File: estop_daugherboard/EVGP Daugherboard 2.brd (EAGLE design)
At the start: 82.6 x 94.1 mm, 41 parts, among them J1 JST-XH-02-PIN-LONG-PAD, J2 JST-XH-02-PIN-LONG-PAD, J3 JST-XH-03-PIN-LONG-PAD, J4 JST-XH-03-PIN-LONG-PAD, J5 AVR_SPI_PROG_3X2PTH, J6 UX60-MB-5S8, J7 4_XH_JST, Q1 N_FET2, Q2 N_FET1, U1 NL27WZ08USG, U2 ATMEGA32U4-AU, X1 TSX-3225 16.0000MF18X-AC0

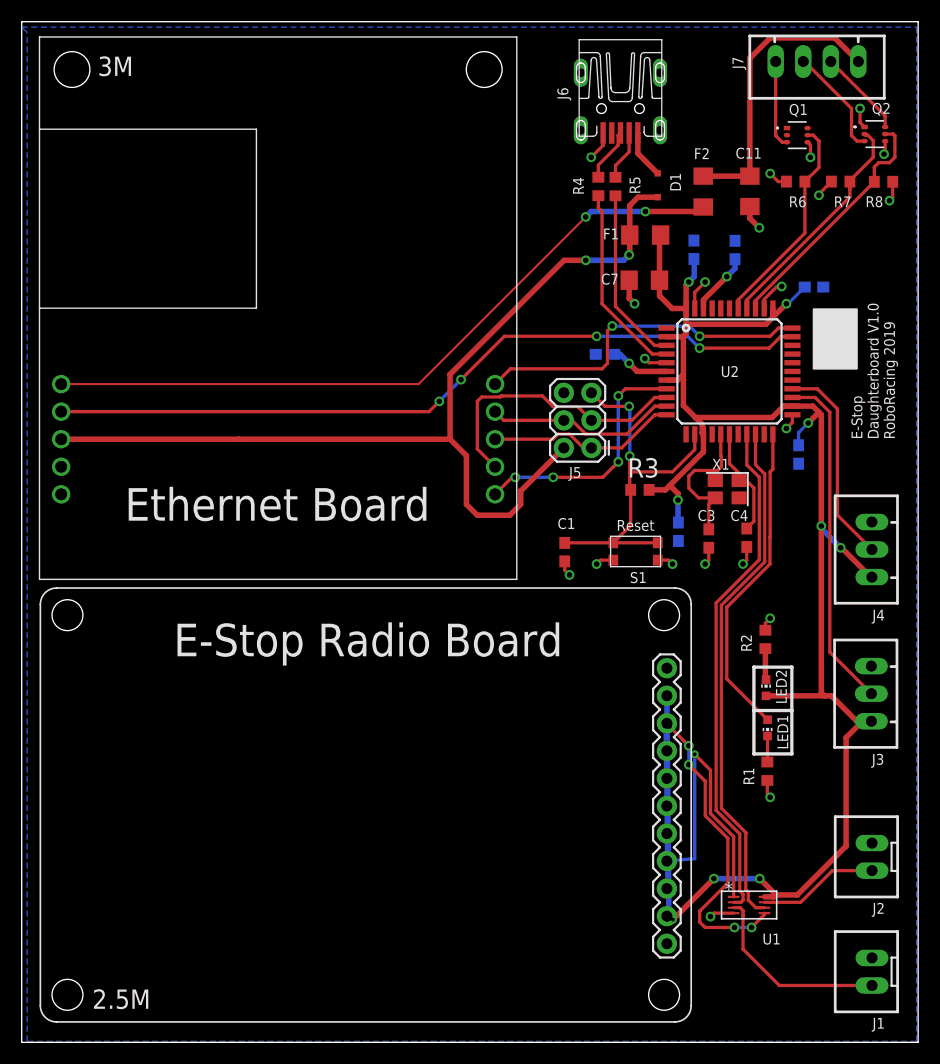
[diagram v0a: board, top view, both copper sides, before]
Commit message: IC silkscreens fixed and switched to merged library
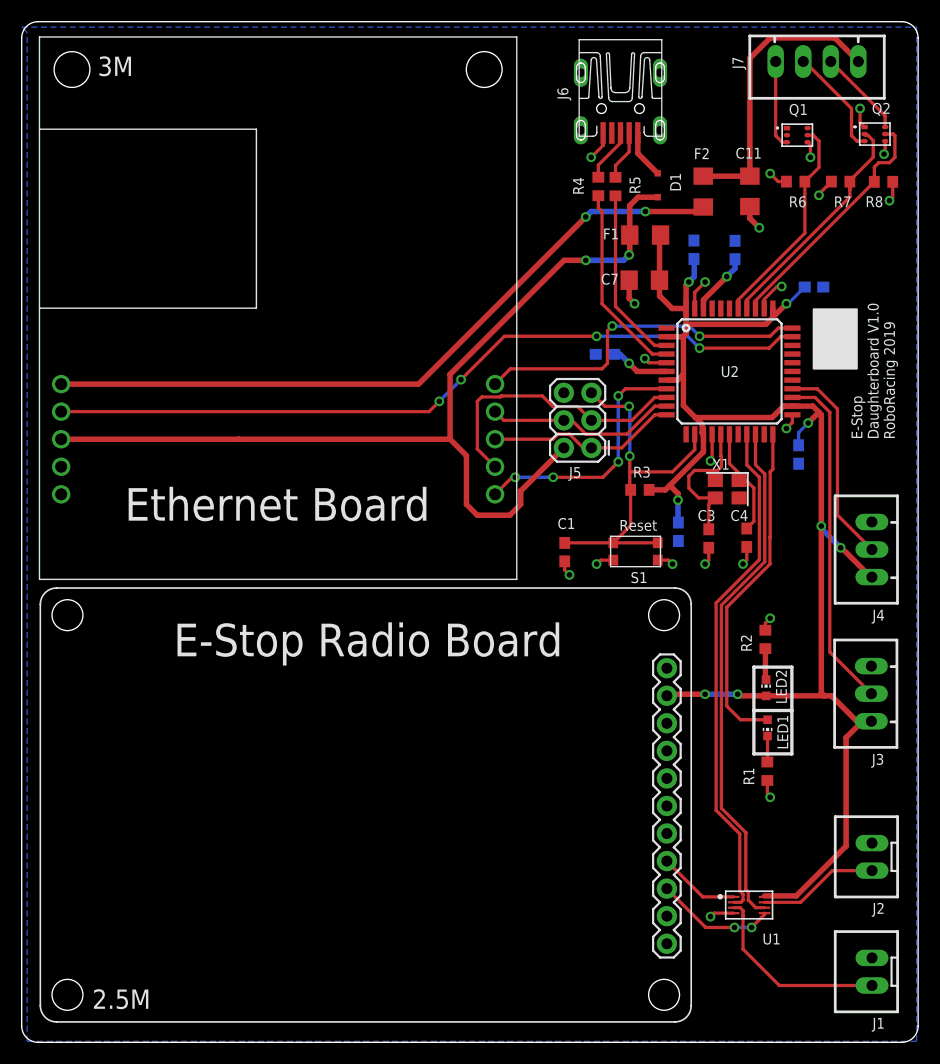
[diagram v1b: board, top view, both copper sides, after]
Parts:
- Q1, Q2: device DownloadedParts:SOT-363 -> Daughterboard-Stuff:SOT-363
- U1: device DownloadedFiles:US8_2P40X2P10 -> Daughterboard-Stuff:US8_2P40X2P10
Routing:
- net DRIVE_EN_RB: track 43.2 -> 11.1 mm, vias 5 -> 2
- net 5V: track 168.0 -> 144.7 mm, vias 9 -> 8
- net STEERING_EN_RB: track 26.8 -> 7.52 mm, vias 1 -> 0
- net GND: track 40.1 -> 42.6 mm, vias 21 -> 22
- net LED1: track 29.6 -> 31.1 mm
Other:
- outline, holes or cut-outs redrawn

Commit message: Fixed the routing widths
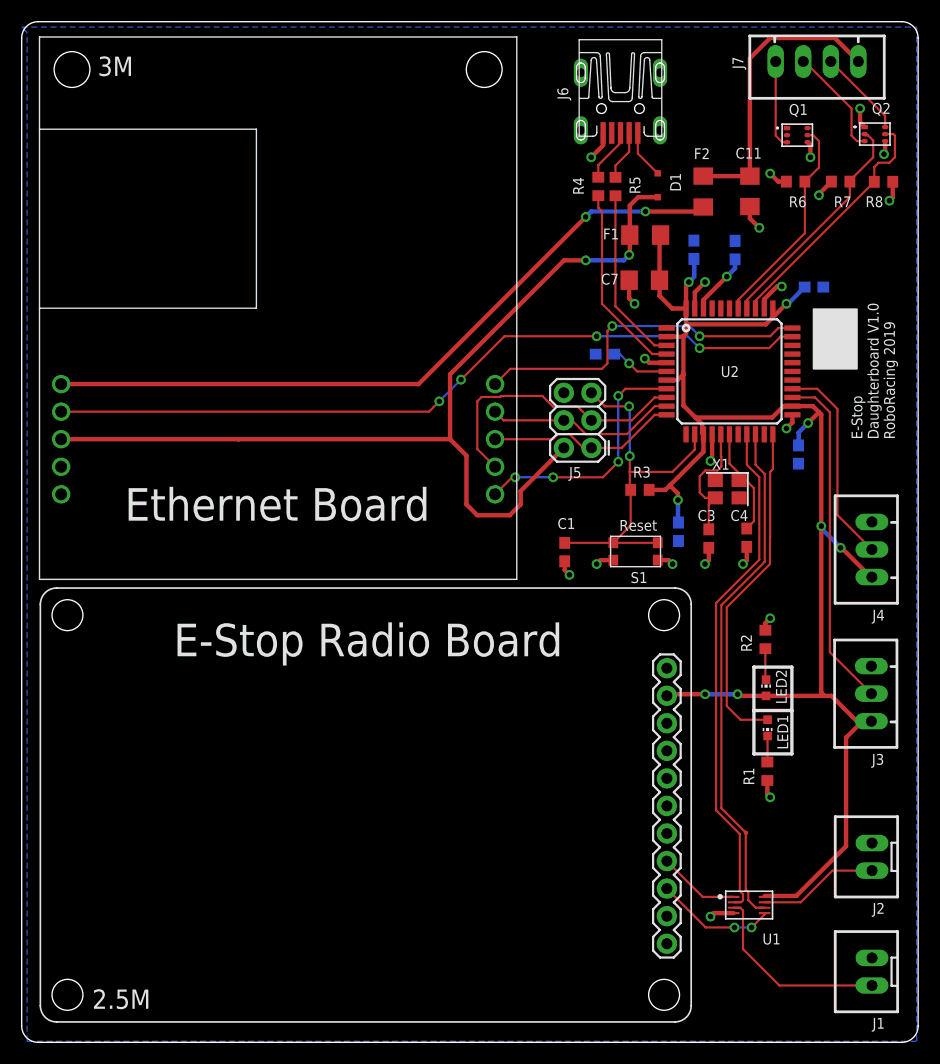
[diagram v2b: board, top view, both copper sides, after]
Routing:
- net XTAL2: track 13.4 -> 11.6 mm

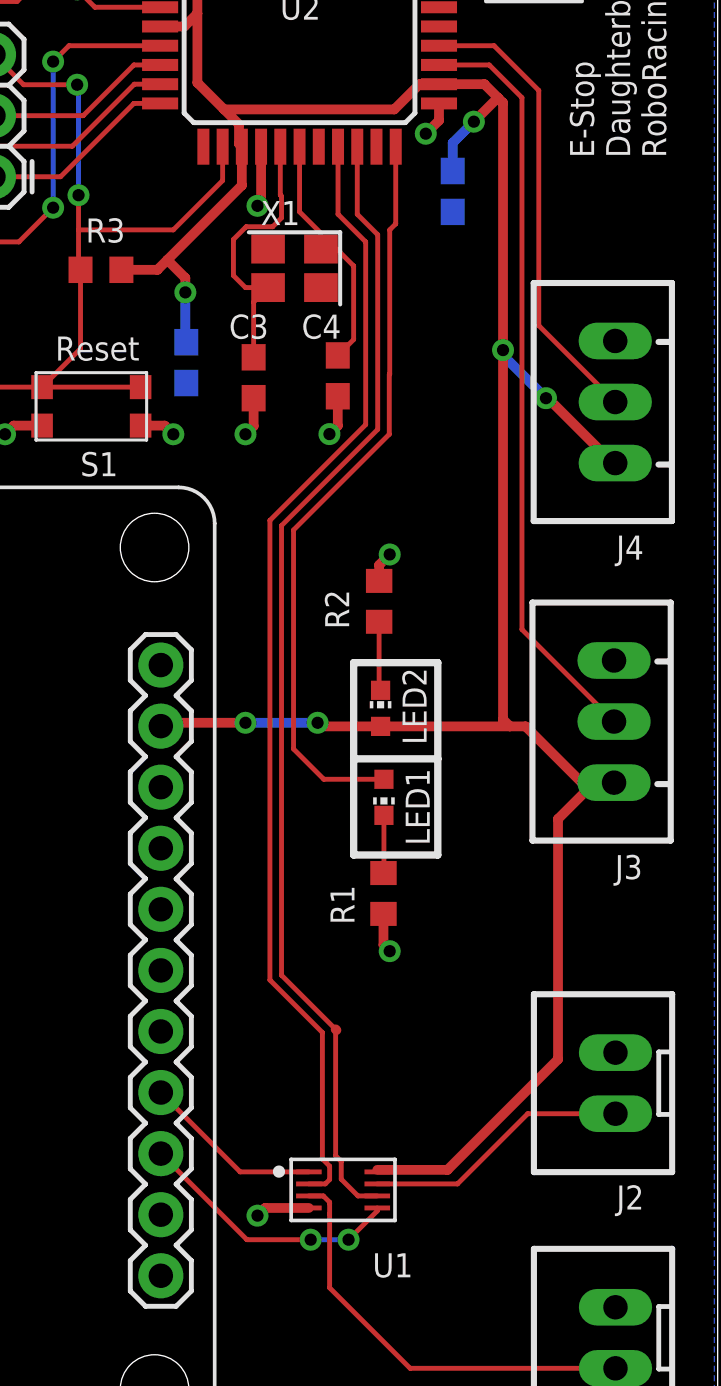
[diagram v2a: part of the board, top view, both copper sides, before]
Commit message: added enable_rb connections to atmega
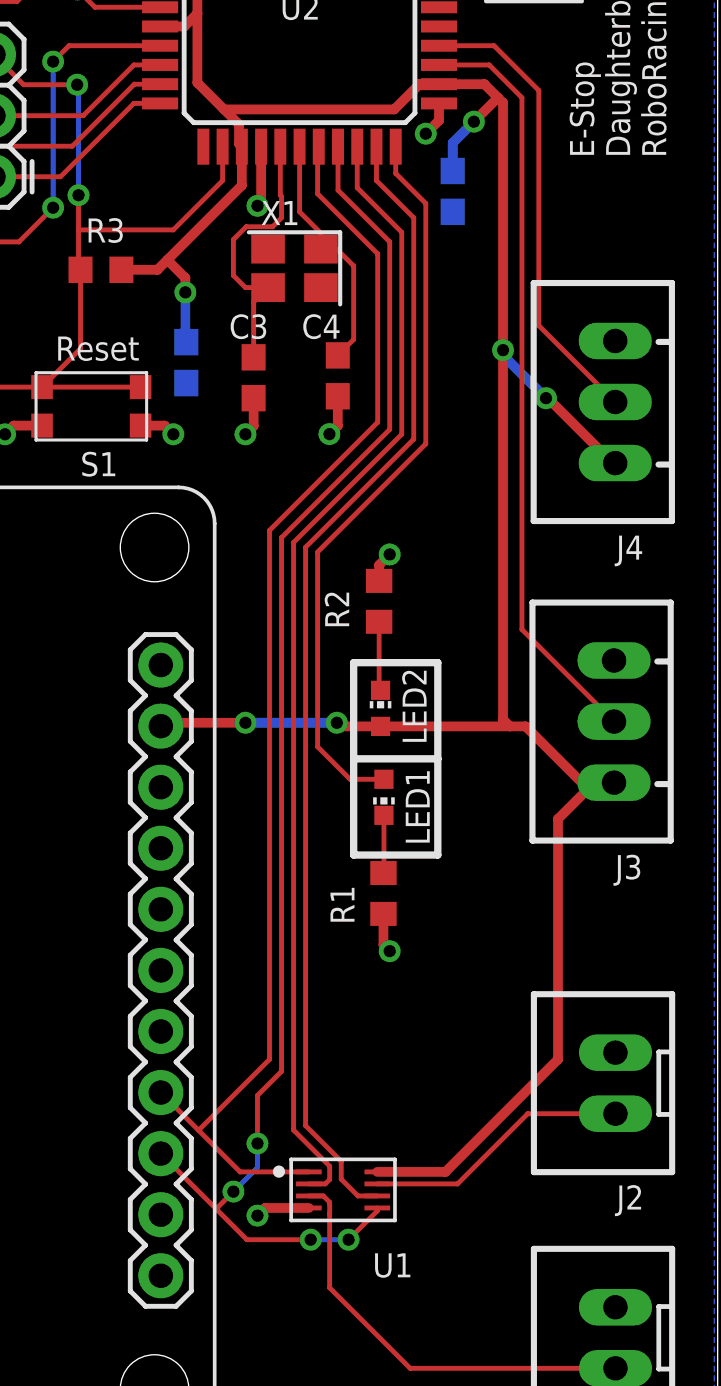
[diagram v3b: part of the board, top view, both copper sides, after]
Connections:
- net DRIVE_EN_DB: now also U2.21; no longer U2.20
- net DRIVE_EN_RB: now also U2.19
- net STEERING_EN_DB: now also U2.20; no longer U2.19
- net STEERING_EN_RB: now also U2.18
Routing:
- net DRIVE_EN_RB: track 11.1 -> 59.2 mm, vias 2 -> 4
- net STEERING_EN_RB: track 7.52 -> 52.6 mm
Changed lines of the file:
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@@
 <?xml version="1.0" encoding="utf-8"?>
 <!DOCTYPE eagle SYSTEM "eagle.dtd">
-<eagle version="9.5.1">
+<eagle version="9.5.0">
 <drawing>
 <settings>
@@
 <wire x1="76.5" y1="62.5" x2="76.5" y2="62.49934375" width="0.4064" layer="1"/>
 <wire x1="76.5" y1="62.49934375" x2="75.25" y2="61.24934375" width="0.4064" layer="1"/>
-<wire x1="77.4042" y1="7.9042" x2="74.4824" y2="7.9042" width="0.4064" layer="1"/>
-<wire x1="82" y1="12.5" x2="77.4042" y2="7.9042" width="0.4064" layer="1"/>
-<wire x1="74.62" y1="26.35" x2="72.15" y2="26.35" width="0.4064" layer="1"/>
-<wire x1="72.15" y1="26.35" x2="72" y2="26.5" width="0.4064" layer="1"/>
-<via x="72" y="26.5" extent="1-16" drill="0.508"/>
-<wire x1="72" y1="26.5" x2="69" y2="26.5" width="0.4064" layer="16"/>
+<wire x1="74.62" y1="26.35" x2="72.95" y2="26.35" width="0.4064" layer="1"/>
+<wire x1="72.95" y1="26.35" x2="72.8" y2="26.5" width="0.4064" layer="1"/>
+<via x="72.8" y="26.5" extent="1-16" drill="0.508"/>
+<wire x1="72.8" y1="26.5" x2="69" y2="26.5" width="0.4064" layer="16"/>
 <via x="69" y="26.5" extent="1-16" drill="0.508"/>
 <wire x1="69" y1="26.5" x2="65.62" y2="26.5" width="0.4064" layer="1"/>
 <wire x1="65.62" y1="26.5" x2="65.48" y2="26.36" width="0.4064" layer="1"/>
-<wire x1="74.4824" y1="7.9042" x2="74.4824" y2="7.82" width="0" layer="19" extent="1-1"/>
+<wire x1="77.32" y1="7.82" x2="74.4824" y2="7.82" width="0.4064" layer="1"/>
+<wire x1="82" y1="12.5" x2="77.32" y2="7.82" width="0.4064" layer="1"/>
 </signal>
 <signal name="MCU_RST">
@@
 <contactref element="LED1" pad="A"/>
 <contactref element="U2" pad="22"/>
-<wire x1="74.76" y1="24.15" x2="72.26" y2="24.15" width="0.2032" layer="1"/>
-<wire x1="72.26" y1="24.15" x2="71" y2="25.41" width="0.2032" layer="1"/>
-<wire x1="71" y1="34.5175" x2="74.9826" y2="38.5001" width="0.2032" layer="1"/>
-<wire x1="74.9826" y1="40.9826" x2="75" y2="41" width="0.2032" layer="1"/>
-<wire x1="74.9826" y1="38.5001" x2="74.9826" y2="40.9826" width="0.2032" layer="1"/>
-<wire x1="75" y1="47" x2="75" y2="41" width="0.2032" layer="1"/>
-<wire x1="71" y1="25.41" x2="71" y2="34.5175" width="0.2032" layer="1"/>
-<wire x1="75.25" y1="50.46" x2="75.25" y2="47.25" width="0.2032" layer="1"/>
-<wire x1="75.25" y1="47.25" x2="75" y2="47" width="0.2032" layer="1"/>
+<wire x1="74.76" y1="24.15" x2="73.35" y2="24.15" width="0.2032" layer="1"/>
+<wire x1="73.35" y1="24.15" x2="72" y2="25.5" width="0.2032" layer="1"/>
+<wire x1="75.25" y1="49.35" x2="75.25" y2="50.46" width="0.2032" layer="1"/>
+<wire x1="72" y1="25.5" x2="72" y2="33.6" width="0.2032" layer="1"/>
+<wire x1="72" y1="33.6" x2="76.5" y2="38.1" width="0.2032" layer="1"/>
+<wire x1="76.5" y1="38.1" x2="76.5" y2="48.1" width="0.2032" layer="1"/>
+<wire x1="76.5" y1="48.1" x2="75.25" y2="49.35" width="0.2032" layer="1"/>
 </signal>
 <signal name="STACK_MCU1">
@@
 <wire x1="74.4824" y1="6.195" x2="74.4824" y2="6.32" width="0.2032" layer="1"/>
 <wire x1="71.7126" y1="5" x2="69.06" y2="5" width="0.2032" layer="1"/>
-<wire x1="69.06" y1="5" x2="65.48" y2="8.58" width="0.2032" layer="1"/>
+<wire x1="69.06" y1="5" x2="67.78" y2="6.28" width="0.2032" layer="1"/>
+<contactref element="U2" pad="19"/>
+<wire x1="67.78" y1="6.28" x2="65.48" y2="8.58" width="0.2032" layer="1"/>
+<wire x1="67.78" y1="6.28" x2="68.5" y2="7" width="0.2032" layer="1"/>
+<via x="68.5" y="7" extent="1-16" drill="0.508"/>
+<wire x1="69.5" y1="8" x2="69.5" y2="9" width="0.2032" layer="16"/>
+<wire x1="69.5" y1="8" x2="68.5" y2="7" width="0.2032" layer="16"/>
+<via x="69.5" y="9" extent="1-16" drill="0.508"/>
+<wire x1="69.5" y1="9" x2="69.5" y2="11" width="0.2032" layer="1"/>
+<wire x1="69.5" y1="11" x2="70.5" y2="12" width="0.2032" layer="1"/>
+<wire x1="70.5" y1="12" x2="70.5" y2="34.2" width="0.2032" layer="1"/>
+<wire x1="70.5" y1="34.2" x2="75" y2="38.7" width="0.2032" layer="1"/>
+<wire x1="72.85" y1="48.65" x2="72.85" y2="50.46" width="0.2032" layer="1"/>
+<wire x1="75" y1="38.7" x2="75" y2="46.5" width="0.2032" layer="1"/>
+<wire x1="75" y1="46.5" x2="72.85" y2="48.65" width="0.2032" layer="1"/>
 </signal>
 <signal name="STEERING_EN_RB">
@@
 <contactref element="RADIO" pad="4"/>
 <wire x1="71.6376" y1="7.82" x2="68.78" y2="7.82" width="0.2032" layer="1"/>
-<wire x1="68.78" y1="7.82" x2="65.48" y2="11.12" width="0.2032" layer="1"/>
+<wire x1="68.78" y1="7.82" x2="67.05" y2="9.55" width="0.2032" layer="1"/>
+<contactref element="U2" pad="18"/>
+<wire x1="67.05" y1="9.55" x2="65.48" y2="11.12" width="0.2032" layer="1"/>
+<wire x1="67.05" y1="9.55" x2="70" y2="12.5" width="0.2032" layer="1"/>
+<wire x1="70" y1="34.5" x2="74.5" y2="39" width="0.2032" layer="1"/>
+<wire x1="74.5" y1="39" x2="74.5" y2="46" width="0.2032" layer="1"/>
+<wire x1="74.5" y1="46" x2="72" y2="48.5" width="0.2032" layer="1"/>
+<wire x1="72" y1="48.5" x2="72" y2="50.41" width="0.2032" layer="1"/>
+<wire x1="72" y1="50.41" x2="72.05" y2="50.46" width="0.2032" layer="1"/>
+<wire x1="70" y1="12.5" x2="70" y2="34.5" width="0.2032" layer="1"/>
 </signal>
 <signal name="DRIVE_EN_DB">
 <contactref element="U1" pad="6"/>
-<contactref element="U2" pad="20"/>
-<wire x1="73.65" y1="50.46" x2="73.65" y2="47.65" width="0.2032" layer="1"/>
-<wire x1="73.65" y1="47.65" x2="74.5" y2="46.8" width="0.2032" layer="1"/>
-<wire x1="74.5" y1="46.8" x2="74.5" y2="38.7" width="0.2032" layer="1"/>
-<wire x1="74.5" y1="38.7" x2="70.5" y2="34.7" width="0.2032" layer="1"/>
-<wire x1="70.5" y1="16" x2="70.5" y2="34.7" width="0.2032" layer="1"/>
 <wire x1="74.4824" y1="6.82" x2="73.68" y2="6.82" width="0.2032" layer="1"/>
-<wire x1="72.7838" y1="13.7162" x2="72.75" y2="13.75" width="0.4064" layer="1"/>
-<wire x1="72.75" y1="13.75" x2="70.5" y2="16" width="0.2032" layer="1"/>
 <wire x1="73.68" y1="6.82" x2="72.9838" y2="7.5162" width="0.2032" layer="1"/>
-<wire x1="72.9838" y1="8.258275" x2="72.75" y2="8.492075" width="0.2032" layer="1"/>
-<wire x1="72.75" y1="8.492075" x2="72.75" y2="13.75" width="0.2032" layer="1"/>
 <wire x1="72.9838" y1="7.5162" x2="72.9838" y2="8.258275" width="0.2032" layer="1"/>
+<contactref element="U2" pad="21"/>
+<wire x1="72.9838" y1="8.258275" x2="71.5" y2="9.742075" width="0.2032" layer="1"/>
+<wire x1="74.45" y1="49.05" x2="74.45" y2="50.46" width="0.2032" layer="1"/>
+<wire x1="71.5" y1="9.742075" x2="71.5" y2="33.8" width="0.2032" layer="1"/>
+<wire x1="71.5" y1="33.8" x2="76" y2="38.3" width="0.2032" layer="1"/>
+<wire x1="76" y1="38.3" x2="76" y2="47.5" width="0.2032" layer="1"/>
+<wire x1="76" y1="47.5" x2="74.45" y2="49.05" width="0.2032" layer="1"/>
 </signal>
 <signal name="STEERING_EN_DB">
 <contactref element="U1" pad="2"/>
-<contactref element="U2" pad="19"/>
-<wire x1="72.85" y1="50.46" x2="72.85" y2="47.65" width="0.2032" layer="1"/>
-<wire x1="72.85" y1="47.65" x2="74" y2="46.5" width="0.2032" layer="1"/>
-<wire x1="74" y1="46.5" x2="74" y2="38.9" width="0.2032" layer="1"/>
-<wire x1="70.0174" y1="34.9174" x2="74" y2="38.9" width="0.2032" layer="1"/>
 <wire x1="71.6376" y1="7.32" x2="72.32" y2="7.32" width="0.2032" layer="1"/>
-<wire x1="72.5012" y1="8.058375" x2="72.2" y2="8.359575" width="0.2032" layer="1"/>
-<wire x1="72.2" y1="13.6175" x2="70.0174" y2="15.8001" width="0.2032" layer="1"/>
-<wire x1="70.0174" y1="15.8001" x2="70.0174" y2="34.9174" width="0.2032" layer="1"/>
 <wire x1="72.32" y1="7.32" x2="72.5012" y2="7.5012" width="0.2032" layer="1"/>
 <wire x1="72.5012" y1="7.5012" x2="72.5012" y2="8.058375" width="0.2032" layer="1"/>
-<wire x1="72.2" y1="8.359575" x2="72.2" y2="13.6175" width="0.2032" layer="1"/>
+<contactref element="U2" pad="20"/>
+<wire x1="72.5012" y1="8.058375" x2="71" y2="9.559575" width="0.2032" layer="1"/>
+<wire x1="71" y1="34" x2="75.5" y2="38.5" width="0.2032" layer="1"/>
+<wire x1="71" y1="9.559575" x2="71" y2="34" width="0.2032" layer="1"/>
+<wire x1="75.5" y1="38.5" x2="75.5" y2="46.9" width="0.2032" layer="1"/>
+<wire x1="73.65" y1="48.75" x2="73.65" y2="50.46" width="0.2032" layer="1"/>
+<wire x1="75.5" y1="46.9" x2="73.65" y2="48.75" width="0.2032" layer="1"/>
 </signal>
 <signal name="STEERING_EN">
